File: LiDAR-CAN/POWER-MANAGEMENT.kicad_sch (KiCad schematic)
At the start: 0 parts

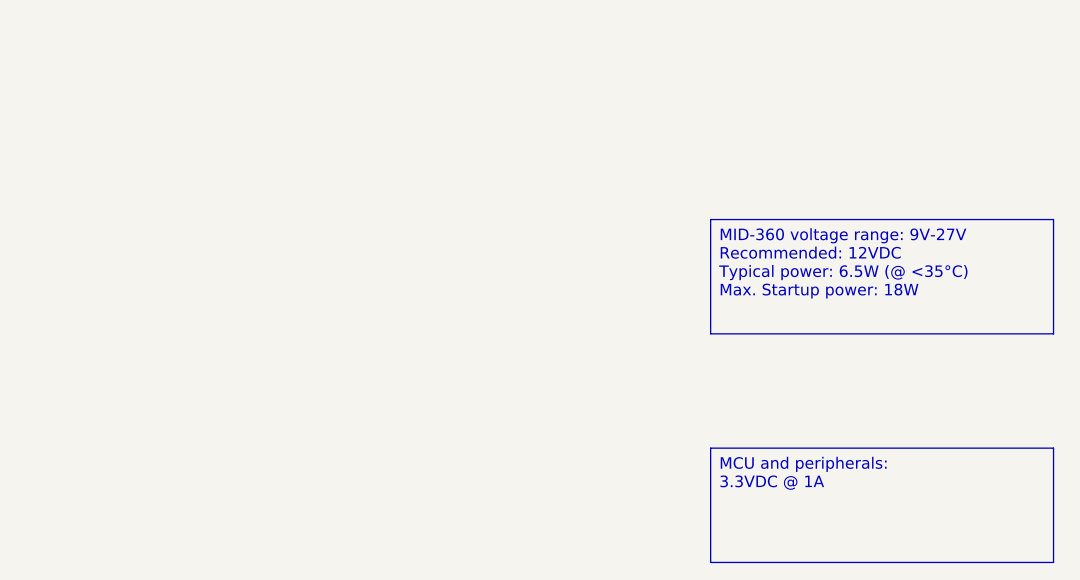
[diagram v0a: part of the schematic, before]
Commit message: Add main components in schematic sheets
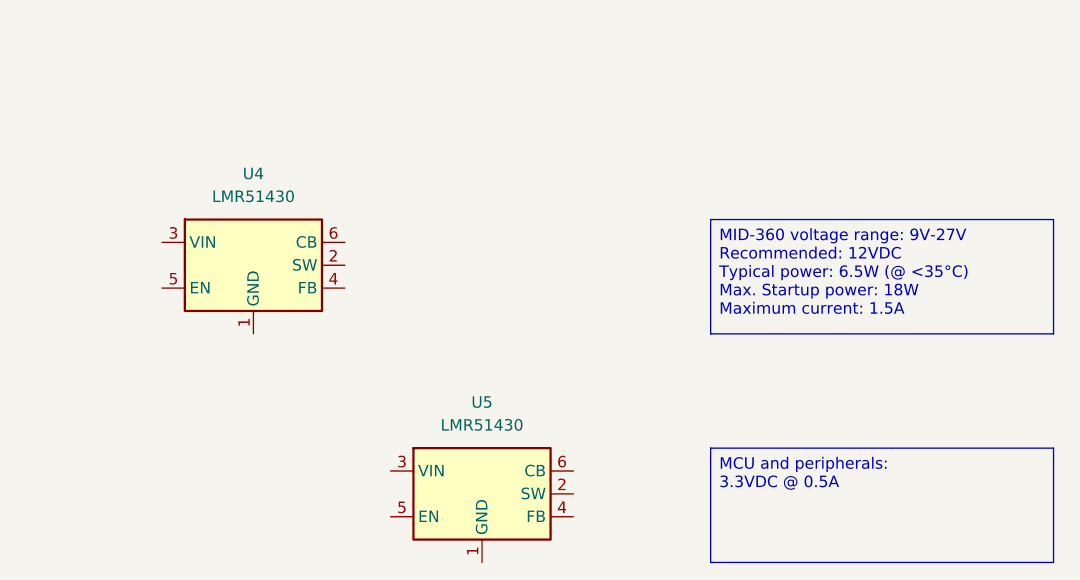
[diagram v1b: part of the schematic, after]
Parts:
- added U4, U5: LMR51430, Package_TO_SOT_SMD:SOT-23-6, symbol Regulator_Switching:LMR51430
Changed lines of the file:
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@@
 		)
 	)
-	(text_box "MID-360 voltage range: 9V-27V\nRecommended: 12VDC\nTypical power: 6.5W (@ <35°C)\nMax. Startup power: 18W  "
+	(text_box "MID-360 voltage range: 9V-27V\nRecommended: 12VDC\nTypical power: 6.5W (@ <35°C)\nMax. Startup power: 18W\nMaximum current: 1.5A"
 		(exclude_from_sim no)
 		(at 190.5 50.8 0)
@@
 		)
 	)
-	(text_box "MCU and peripherals:\n3.3VDC @ 1A"
+	(text_box "MCU and peripherals:\n3.3VDC @ 0.5A"
 		(exclude_from_sim no)
 		(at 190.5 76.2 0)
@@
 		)
 	)
+	(symbol
+		(lib_id "Regulator_Switching:LMR51430")
+		(at 165.1 81.28 0)
+		(unit 1)
+		(exclude_from_sim no)
+		(in_bom yes)
+		(on_board yes)
+		(dnp no)
+		(fields_autoplaced yes)
+		(property "Reference" "U5"
+			(at 165.1 71.12 0)
+			(effects
+				(font
+					(size 1.27 1.27)
+				)
+			)
+		)
+		(property "Value" "LMR51430"
+			(at 165.1 73.66 0)
+			(effects
+				(font
+					(size 1.27 1.27)
+				)
+			)
+		)
+		(property "Footprint" "Package_TO_SOT_SMD:SOT-23-6"
+			(at 166.37 90.17 0)
+			(effects
+				(font
+					(size 1.27 1.27)
+				)
+				(justify left)
+				(hide yes)
+			)
+		)
+		(property "Datasheet" "https://www.ti.com/lit/ds/symlink/lmr51430.pdf"
+			(at 166.37 92.71 0)
+			(effects
+				(font
+					(size 1.27 1.27)
+				)
+				(justify left)
+				(hide yes)
+			)
+		)
+		(property "Description" "4.5-V to 36-V, 3-A synchronous buck converter with 40-µA IQ, SOT-23-6"
+			(at 165.1 81.28 0)
+			(effects
+				(font
+					(size 1.27 1.27)
+				)
+				(hide yes)
+			)
+		)
+		(pin "5"
+		)
+		(pin "1"
+		)
+		(pin "3"
+		)
+		(pin "6"
+		)
+		(pin "2"
+		)
+		(pin "4"
+		)
+		(instances
+			(project ""
+				(path "/56db6f21-0e4a-4321-bd8a-db37f1842dd9/279681b5-dc02-4bbb-98e2-e427440df0b4"
+					(reference "U5")
+					(unit 1)
+				)
+			)
+		)
+	)
+	(symbol
+		(lib_id "Regulator_Switching:LMR51430")
+		(at 139.7 55.88 0)
+		(unit 1)
+		(exclude_from_sim no)
+		(in_bom yes)
+		(on_board yes)
+		(dnp no)
+		(fields_autoplaced yes)
+		(property "Reference" "U4"
+			(at 139.7 45.72 0)
+			(effects
+				(font
+					(size 1.27 1.27)
+				)
+			)
+		)
+		(property "Value" "LMR51430"
+			(at 139.7 48.26 0)
+			(effects
+				(font
+					(size 1.27 1.27)
+				)
+			)
+		)
+		(property "Footprint" "Package_TO_SOT_SMD:SOT-23-6"
+			(at 140.97 64.77 0)
+			(effects
+				(font
+					(size 1.27 1.27)
+				)
+				(justify left)
+				(hide yes)
+			)
+		)
+		(property "Datasheet" "https://www.ti.com/lit/ds/symlink/lmr51430.pdf"
+			(at 140.97 67.31 0)
+			(effects
+				(font
+					(size 1.27 1.27)
+				)
+				(justify left)
+				(hide yes)
+			)
+		)
+		(property "Description" "4.5-V to 36-V, 3-A synchronous buck converter with 40-µA IQ, SOT-23-6"
+			(at 139.7 55.88 0)
+			(effects
+				(font
+					(size 1.27 1.27)
+				)
+				(hide yes)
+			)
+		)
+		(pin "6"
+		)
+		(pin "2"
+		)
+		(pin "1"
+		)
+		(pin "4"
+		)
+		(pin "3"
+		)
+		(pin "5"
+		)
+		(instances
+			(project ""
+				(path "/56db6f21-0e4a-4321-bd8a-db37f1842dd9/279681b5-dc02-4bbb-98e2-e427440df0b4"
+					(reference "U4")
+					(unit 1)
+				)
+			)
+		)
+	)

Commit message: Add LiDAR Interface complete circuit
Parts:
- U4, U5: MPN (none) -> LMR51430XDDCR; Manufacturer (none) -> Texas Instruments
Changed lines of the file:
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@@
+			)
+		)
+		(property "Manufacturer" "Texas Instruments"
+			(at 165.1 81.28 0)
+			(effects
+				(font
+					(size 1.27 1.27)
+				)
+				(hide yes)
+			)
+		)
+		(property "MPN" "LMR51430XDDCR"
+			(at 165.1 81.28 0)
+			(effects
+				(font
+					(size 1.27 1.27)
+				)
+				(hide yes)
 			)
 		)
@@
 			(at 139.7 55.88 0)
 			(effects
+				(font
+					(size 1.27 1.27)
+				)
+				(hide yes)
+			)
+		)
+		(property "Manufacturer" "Texas Instruments"
+			(at 139.7 55.88 0)
+			(effects
+				(font
+					(size 1.27 1.27)
+				)
+				(hide yes)
+			)
+		)
+		(property "MPN" "LMR51430XDDCR"
+			(at 139.7 55.88 0)
+			(effects

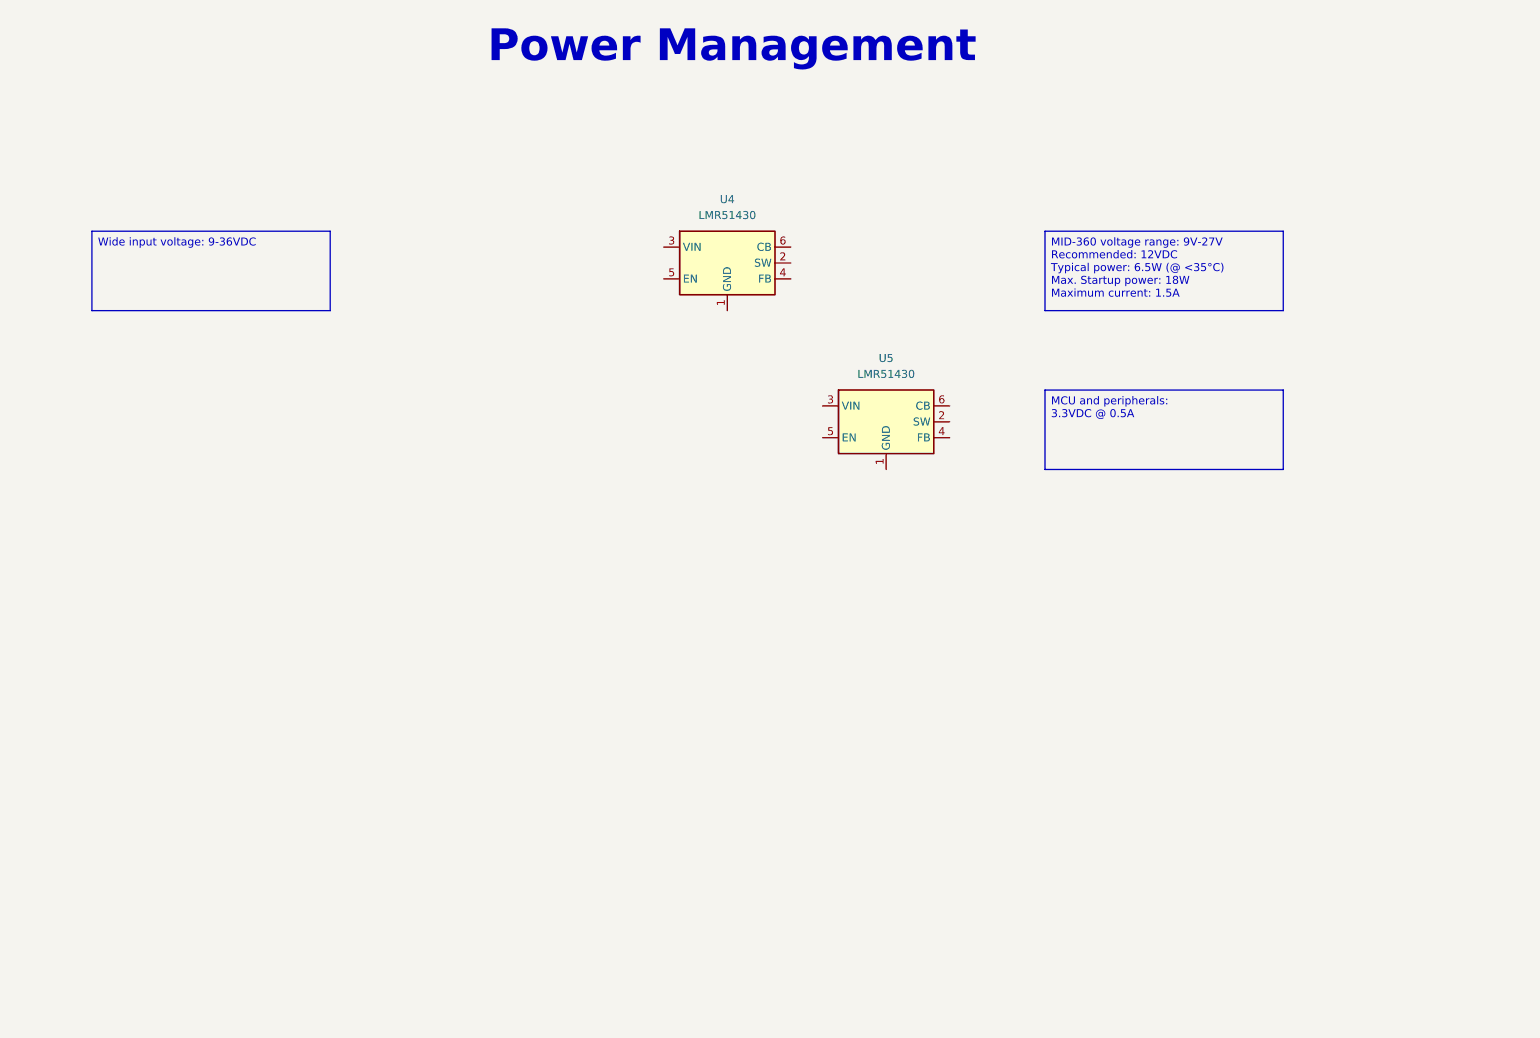
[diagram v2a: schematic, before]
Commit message: Add power management circuit
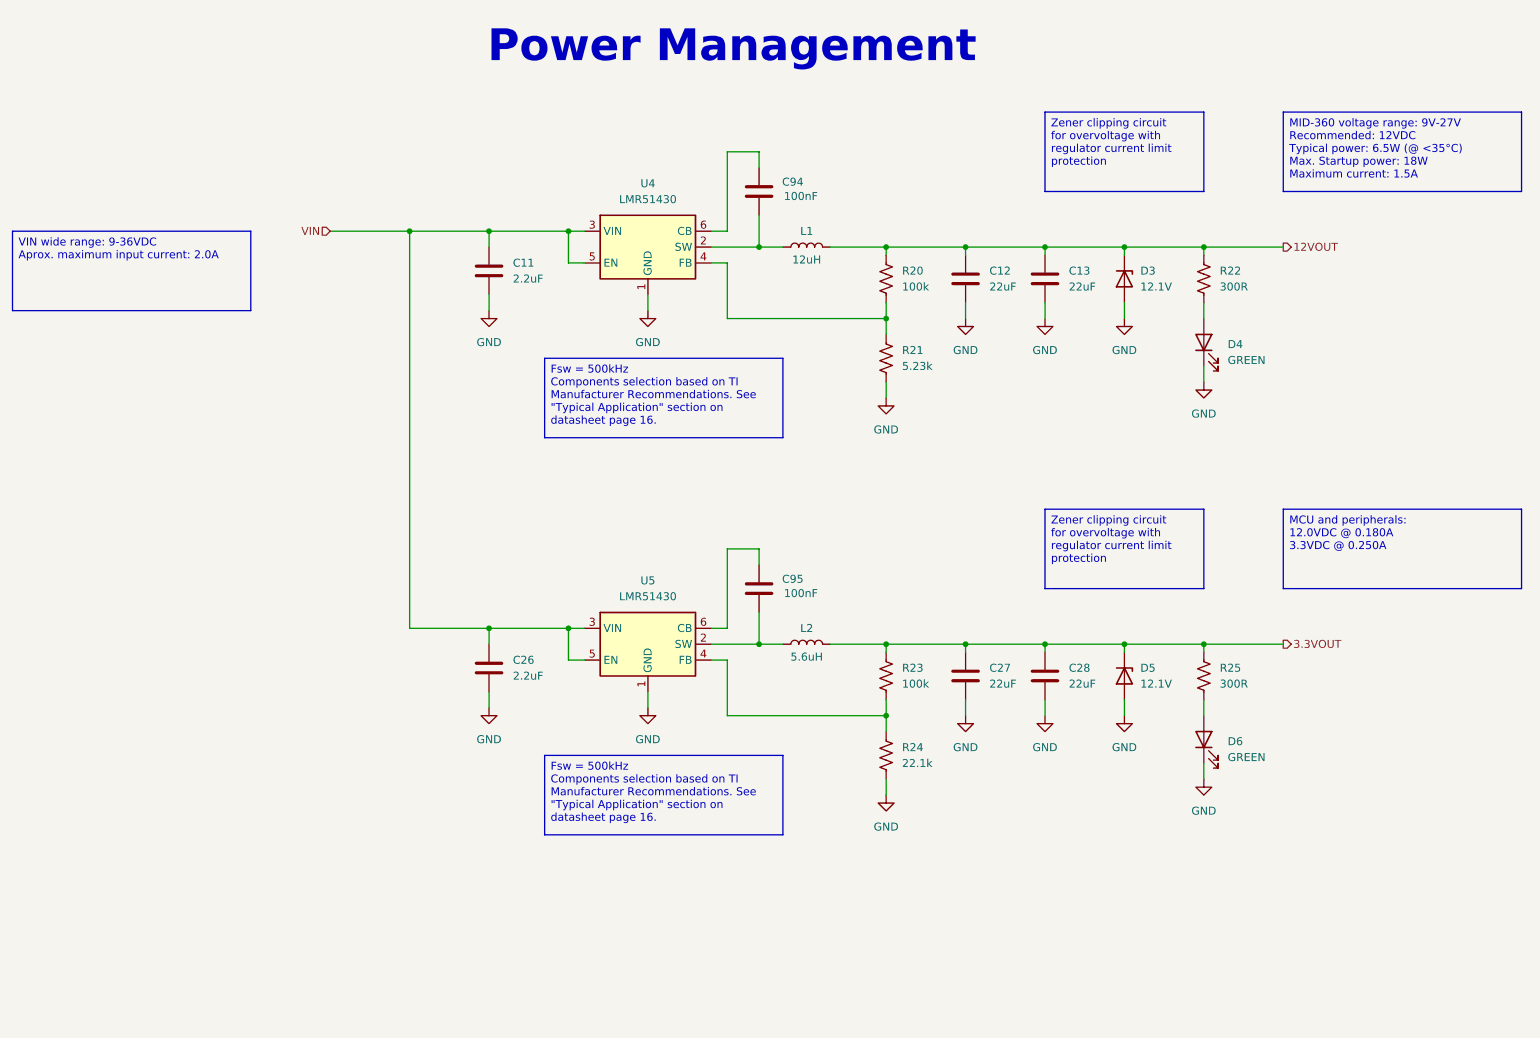
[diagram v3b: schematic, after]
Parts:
- added C11, C26: 2.2uF, Capacitor_SMD:C_0805_2012Metric, symbol Device:C
- added C12, C13, C27, C28: 22uF, Capacitor_SMD:C_0805_2012Metric, symbol Device:C
- added C94, C95: 100nF, Capacitor_SMD:C_0603_1608Metric, symbol Symbols:CAP CER 0.1UF 50V X7R 0603
- added D3, D5: 12.1V, Diode_SMD:D_SMA, symbol Device:D_Zener
- added D4, D6: GREEN, LED_SMD:LED_0603_1608Metric, symbol Device:LED
- added L1: 12uH, Inductor_SMD:L_APV_ANR6020, symbol Device:L
- added L2: 5.6uH, Inductor_SMD:L_APV_ANR3015, symbol Device:L
- added R20, R23: 100k, Resistor_SMD:R_0603_1608Metric, symbol Device:R_US
- added R21: 5.23k, Resistor_SMD:R_0603_1608Metric, symbol Device:R_US
- added R22, R25: 300R, Resistor_SMD:R_0603_1608Metric, symbol Device:R_US
- added R24: 22.1k, Resistor_SMD:R_0603_1608Metric, symbol Device:R_US
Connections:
- net GND: now reaches U5.1 (GND)
- net GND: now also U4.1 (GND), C11.2, C12.2, C13.2, C26.2, C27.2, C28.2, D3.2 (A), D4.1 (K), D5.2 (A), D6.1 (K), R21.2, R24.2
- net at U5.2 (SW): now also C95.1, L2.1
- net VIN: now reaches U5.3 (VIN)
- net VIN: now also U4.3 (VIN), U4.5 (EN), U5.5 (EN), C11.1, C26.1
- net at U5.4 (FB): now also R23.2, R24.1
- net at U5.6 (CB): now also C95.2
- net at U4.2 (SW): now also C94.1, L1.1
- net at U4.4 (FB): now also R20.2, R21.1
- net at U4.6 (CB): now also C94.2
- new net: D4.2 (A), R22.2
- new net: D6.2 (A), R25.2
- new net 12VOUT: C12.1, C13.1, D3.1 (K), L1.2, R20.1, R22.1
- new net 3.3VOUT: C27.1, C28.1, D5.1 (K), L2.2, R23.1, R25.1
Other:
- moved on the sheet: U4

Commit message: Add power management connections in Root sheet
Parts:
- D5: value 12.1V -> 5.1V; MPN 1SMA5927BT3G -> SMAZ5V1-13-F; Manufacturer onsemi -> Diodes Incorporated
- Dw: renamed from D3; value 12.1V -> 12V
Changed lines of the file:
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@@
 			)
 		)
-		(property "Value" "12.1V"
+		(property "Value" "5.1V"
 			(at 205.74 123.1899 90)
 			(effects
@@
 			)
 		)
-		(property "Datasheet" "https://www.onsemi.com/pdf/datasheet/1sma5913bt3-d.pdf"
+		(property "Datasheet" "https://www.diodes.com/assets/Datasheets/ds18015.pdf"
 			(at 203.2 121.92 0)
 			(effects
@@
 			)
 		)
-		(property "Description" "DIODE ZENER 12V 1.5W SMA"
+		(property "Description" "DIODE ZENER 5.1V 1W SMA"
 			(at 203.2 121.92 0)
 			(effects
@@
 			)
 		)
-		(property "Manufacturer" "onsemi"
+		(property "Manufacturer" "Diodes Incorporated"
 			(at 203.2 121.92 90)
 			(effects
@@
 			)
 		)
-		(property "MPN" "1SMA5927BT3G"
+		(property "MPN" "SMAZ5V1-13-F"
 			(at 203.2 121.92 90)
 			(effects
@@
 		(dnp no)
 		(fields_autoplaced yes)
-		(property "Reference" "D3"
+		(property "Reference" "Dw"
 			(at 205.74 57.1499 90)
 			(effects
@@
 			)
 		)
-		(property "Value" "12.1V"
+		(property "Value" "12V"
 			(at 205.74 59.6899 90)
 			(effects
@@
 			(project ""
 				(path "/56db6f21-0e4a-4321-bd8a-db37f1842dd9/279681b5-dc02-4bbb-98e2-e427440df0b4"
-					(reference "D3")
-					(unit 1)
-				)
+					(reference "Dw")
+					(unit 1)
+				)

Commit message: Feature schematic revision 1
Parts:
- added TP10, TP11, TP12, TP13, TP14, TP15, TP16, TP9: TestPoint, TestPoint:TestPoint_Pad_D1.5mm, symbol Connector:TestPoint
- renumbered C95 to C10, C26 to C11, C27 to C12, C28 to C13, C94 to C6, C11 to C7, C12 to C8, C13 to C9, D4 to D2, D5 to D3, D6 to D4, Dw to Dw1, R20 to R11, R22 to R12, R21 to R13, R23 to R14, R25 to R15, R24 to R16, U4 to U1, U5 to U2
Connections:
- net 12VOUT: now also TP15.1
- net 3.3VOUT: now also TP16.1
- net VIN: now also TP10.1, TP9.1
- net SW_3V3: now reaches C10.1, L2.1, U2.2 (SW)
- net SW_3V3: now also TP13.1
- net SW_12V: now reaches C6.1, L1.1, U1.2 (SW)
- net SW_12V: now also TP11.1
- net FB_3V3: now reaches R14.2, R16.1, U2.4 (FB)
- net FB_3V3: now also TP14.1
- net FB_12V: now reaches R11.2, R13.1, U1.4 (FB)
- net FB_12V: now also TP12.1

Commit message: Start placement of components
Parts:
- TP10, TP11, TP12, TP13, TP14, TP15, TP16, TP9: footprint TestPoint:TestPoint_Pad_D1.5mm -> TestPoint:TestPoint_Pad_D1.0mm
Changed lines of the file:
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@@
 		(exclude_from_sim no)
 		(in_bom no)
-		(on_board no)
+		(on_board yes)
 		(dnp no)
 		(fields_autoplaced yes)
@@
 			)
 		)
-		(property "Footprint" "TestPoint:TestPoint_Pad_D1.5mm"
+		(property "Footprint" "TestPoint:TestPoint_Pad_D1.0mm"
 			(at 106.68 162.56 0)
 			(effects
@@
 		(exclude_from_sim no)
 		(in_bom no)
-		(on_board no)
+		(on_board yes)
 		(dnp no)
 		(fields_autoplaced yes)
@@
 			)
 		)
-		(property "Footprint" "TestPoint:TestPoint_Pad_D1.5mm"
+		(property "Footprint" "TestPoint:TestPoint_Pad_D1.0mm"
 			(at 93.98 162.56 0)
 			(effects
@@
 		(exclude_from_sim no)
 		(in_bom no)
-		(on_board no)
+		(on_board yes)
 		(dnp no)
 		(fields_autoplaced yes)
@@
 			)
 		)
-		(property "Footprint" "TestPoint:TestPoint_Pad_D1.5mm"
+		(property "Footprint" "TestPoint:TestPoint_Pad_D1.0mm"
 			(at 68.58 162.56 0)
 			(effects
@@
 		(exclude_from_sim no)
 		(in_bom no)
-		(on_board no)
+		(on_board yes)
 		(dnp no)
 		(fields_autoplaced yes)
@@
 			)
 		)
-		(property "Footprint" "TestPoint:TestPoint_Pad_D1.5mm"
+		(property "Footprint" "TestPoint:TestPoint_Pad_D1.0mm"
 			(at 81.28 162.56 0)
 			(effects
@@
 		(exclude_from_sim no)
 		(in_bom no)
-		(on_board no)
+		(on_board yes)
 		(dnp no)
 		(fields_autoplaced yes)
@@
 			)
 		)
-		(property "Footprint" "TestPoint:TestPoint_Pad_D1.5mm"
+		(property "Footprint" "TestPoint:TestPoint_Pad_D1.0mm"
 			(at 119.38 162.56 0)
 			(effects
@@
 		(exclude_from_sim no)
 		(in_bom no)
-		(on_board no)
+		(on_board yes)
 		(dnp no)
 		(fields_autoplaced yes)
@@
 			)
 		)
-		(property "Footprint" "TestPoint:TestPoint_Pad_D1.5mm"
+		(property "Footprint" "TestPoint:TestPoint_Pad_D1.0mm"
 			(at 55.88 162.56 0)
 			(effects
@@
 		(exclude_from_sim no)
 		(in_bom no)
-		(on_board no)
+		(on_board yes)
 		(dnp no)
 		(fields_autoplaced yes)
@@
 			)
 		)
-		(property "Footprint" "TestPoint:TestPoint_Pad_D1.5mm"
+		(property "Footprint" "TestPoint:TestPoint_Pad_D1.0mm"
 			(at 43.18 162.56 0)
 			(effects
@@
 		(exclude_from_sim no)
 		(in_bom no)
-		(on_board no)
+		(on_board yes)
 		(dnp no)
 		(fields_autoplaced yes)
@@
 			)
 		)
-		(property "Footprint" "TestPoint:TestPoint_Pad_D1.5mm"
+		(property "Footprint" "TestPoint:TestPoint_Pad_D1.0mm"
 			(at 132.08 162.56 0)
 			(effects

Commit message: Complete silkscreen annotation
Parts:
- renumbered Dw1 to D6
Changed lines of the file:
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@@
 		(dnp no)
 		(fields_autoplaced yes)
-		(property "Reference" "Dw1"
+		(property "Reference" "D6"
 			(at 205.74 57.1499 90)
 			(effects
@@
 			(project ""
 				(path "/56db6f21-0e4a-4321-bd8a-db37f1842dd9/279681b5-dc02-4bbb-98e2-e427440df0b4"
-					(reference "Dw1")
+					(reference "D6")
 					(unit 1)
 				)
